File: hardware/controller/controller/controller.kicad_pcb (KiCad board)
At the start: 2 copper layers, 31.8 x 30.5 mm, 9 parts, among them J1 Board Connector, J2 ICSP, J3 Power and Grinder, U1 ATmega328PB-AU

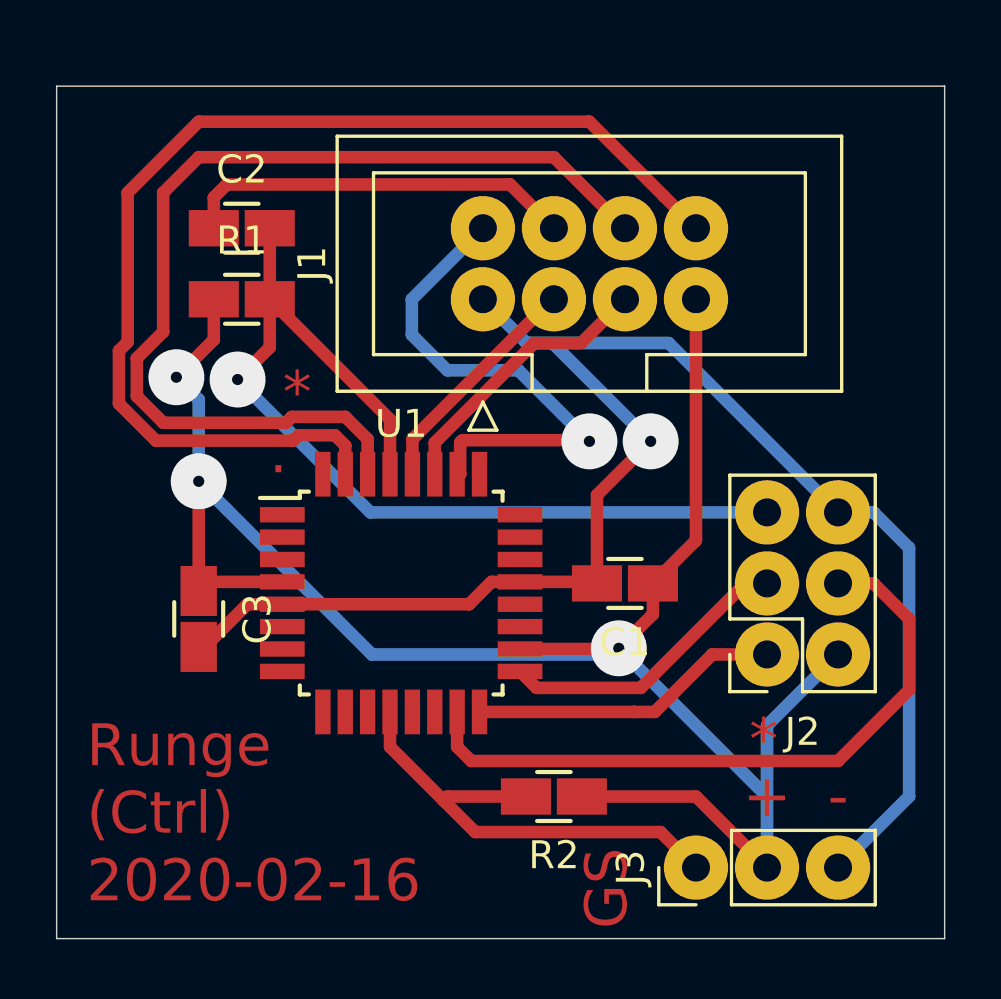
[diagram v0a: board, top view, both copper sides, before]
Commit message: Adding connector for load cell amplifier board.
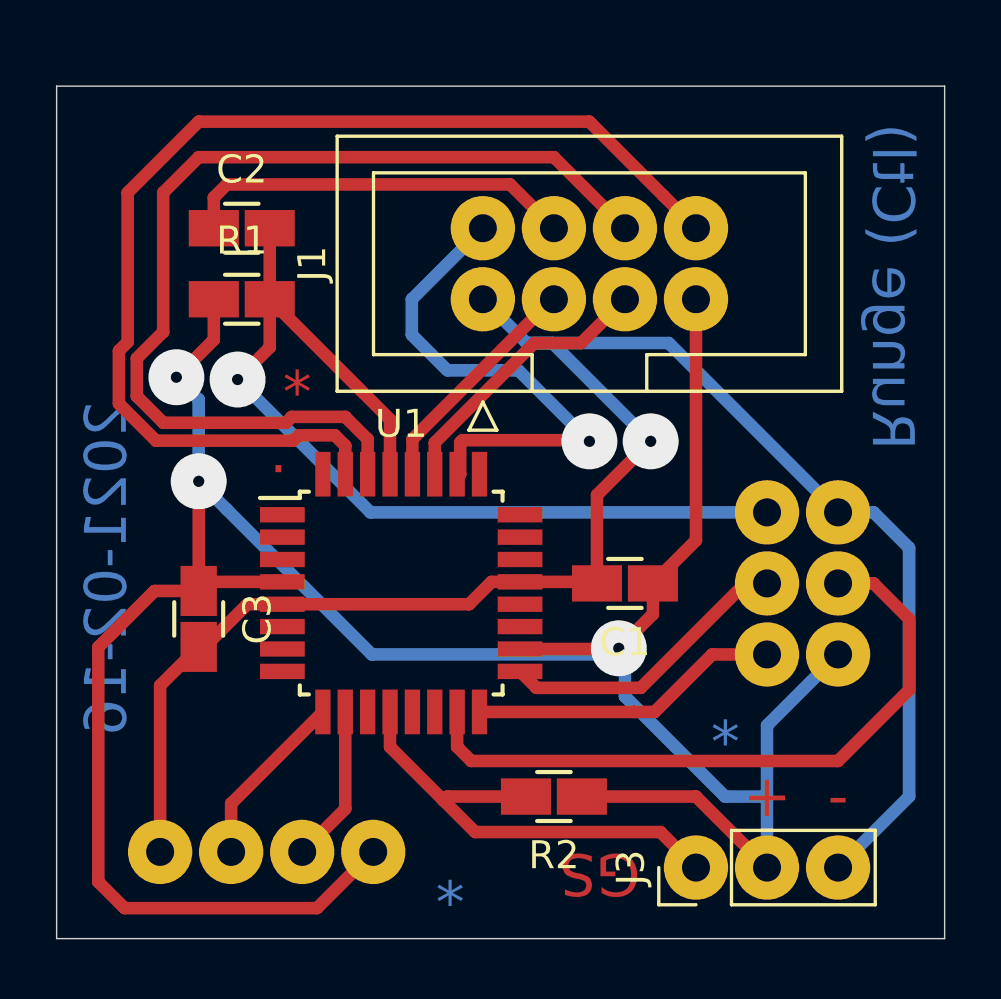
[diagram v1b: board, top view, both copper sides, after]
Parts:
- added J4: Load Cell, Connector_PinHeader_2.54mm:PinHeader_1x04_P2.54mm_Vertical, B.Cu at (140.9, 75.6)
- J2: footprint Connector_PinSocket_2.54mm:PinSocket_2x03_P2.54mm_Vertical -> Connector_PinHeader_2.54mm:PinHeader_2x03_P2.54mm_Vertical; moved to B.Cu
- turned J2 to 0 degrees
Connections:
- U1 pad 10: (no net) -> Net-(J4-Pad2)
- U1 pad 9: (no net) -> Net-(J4-Pad3)
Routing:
- net +5V: track 73.2 -> 98.0 mm
- net GND: track 58.4 -> 66.3 mm
- net Net-(J4-Pad3): track 0.00 -> 6.36 mm
- net Net-(J4-Pad2): track 0.00 -> 5.64 mm
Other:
- board text added: "2021-02-16"
- board text added: "Runge (Ctl)"
- board text removed: "Runge (Ctrl) 2020-02-16"

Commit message: Updating runge controller for new milling process.
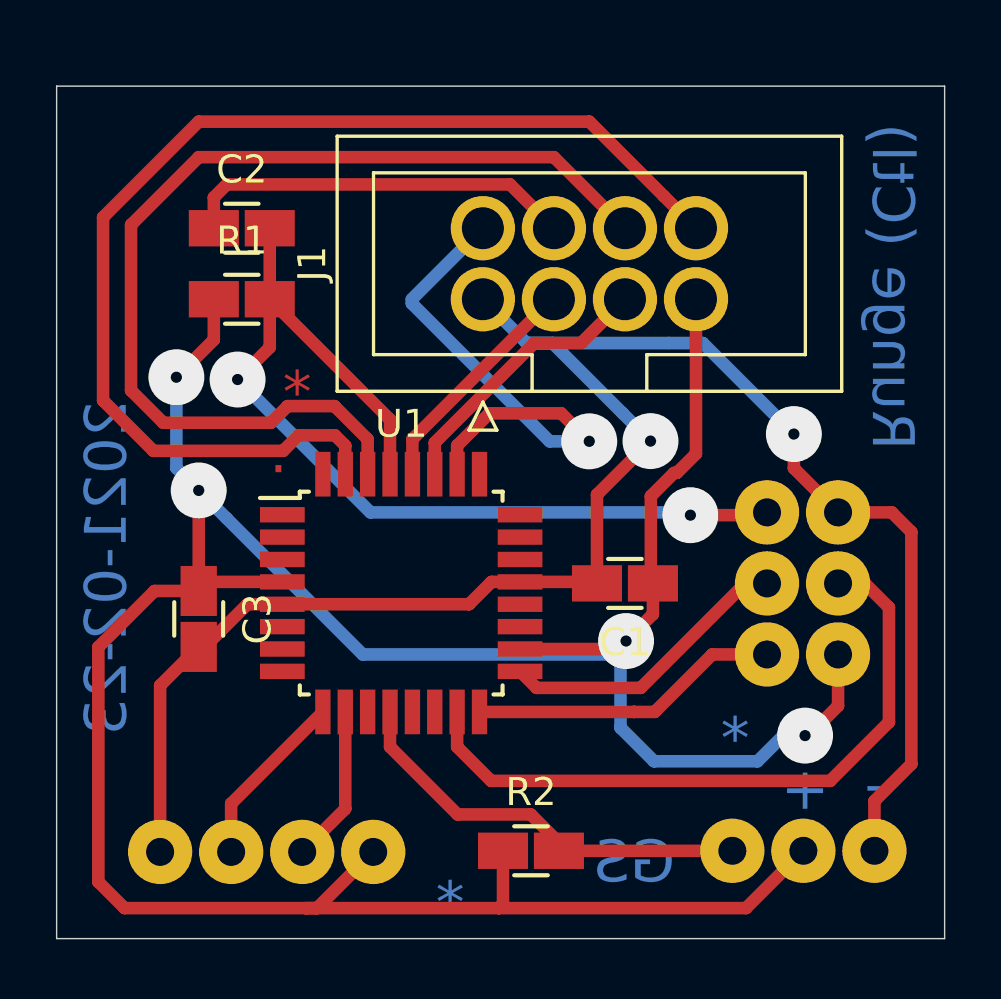
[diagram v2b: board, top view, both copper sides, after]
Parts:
- J3: moved to B.Cu
- moved R2 2.11 mm to (146.5, 75.6), turned to 0 degrees
- moved J3 1.43 mm to (153.7, 75.6), turned to 270 degrees
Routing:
- net +5V: track 98.0 -> 108.9 mm, vias 3 -> 4
- net GRINDER: track 17.0 -> 15.2 mm
- net TXD: track 40.5 -> 41.6 mm
- net RESET: track 34.8 -> 34.9 mm, vias 1 -> 2
- net GND: vias 1 -> 2
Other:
- board text added: "2021-02-23"
- board text removed: "2021-02-16"
